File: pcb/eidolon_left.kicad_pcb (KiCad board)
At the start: 2 copper layers, 117.1 x 83.9 mm, 37 parts

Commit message: fix(pcb): land faithfully re-routed boards + gerbers (corrected pinout)
Replace the old buggy routed boards with the re-routed eidolon_{left,right}
from the phantom autorouter (~/git/phantom-router), built on the corrected
XIAO right-column pinout. Both halves: 0 DRC violations, 0 unconnected.

Whole-module GND pour keepout; explicit hand-shaped B.Cu GND margin rail;
R2/R3 re-derived for the moved pinout (rail crossings on F.Cu, minimal vias);
the mirrored right half's forced GND/RAW crossing and under-MCU access-pad
jumper threaded with one via each. Re-exported gerbers (all layers + drill).

Fab-ready.

Co-Authored-By: Claude Opus 4.8 <noreply@anthropic.com>
Claude-Session: https://claude.ai/code/session_01MD1mhgQXFf8iwVCJGWMS4x
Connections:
- MCU1 pad 10: P3V3 -> D9
- MCU1 pad 12: D9 -> P3V3
- MCU1 pad 13: R3 -> GND
- MCU1 pad 14: R2 -> P5V
- MCU1 pad 8: P5V -> R2
- MCU1 pad 9: GND -> R3
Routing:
- net R2: track 129.9 -> 114.6 mm, vias 1 -> 2
- net R3: track 89.1 -> 80.0 mm, vias 1 -> 2
- net GND: track 159.7 -> 164.2 mm

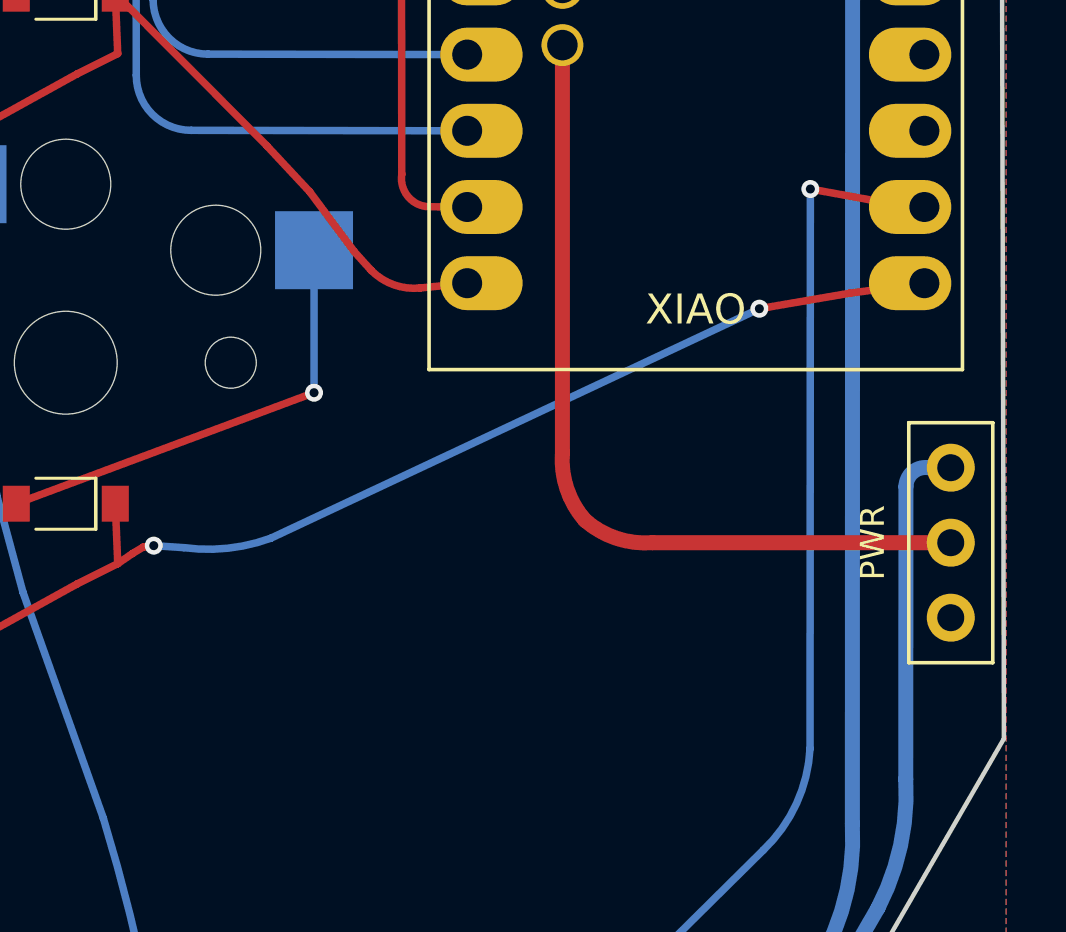
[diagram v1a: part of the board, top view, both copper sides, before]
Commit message: feat(pcb): per-half XIAO pin maps; declutter right-half routing
Each half is an independent wireless unit, so the net->pin maps need not match.
Give the right half its own map (all 4 rows on the matrix-facing D7-D10 edge:
D7:R3 D8:R2 D9:R1 D10:R0; columns on D0-D4). The left keeps R0/R1 on D5/D6.

This moves R0/R1 off the far MCU edge on the right, so they fan out directly
east instead of crossing back over the MCU ("west-about" boxed routes). Only
the 5 columns now cross under the MCU on the right (the physical floor). Both
halves re-routed to 0 DRC / 0 unconnected; gerbers re-exported.

FIRMWARE: the halves now use different MATRIX_ROW_PINS (left D5-D8, right
D7-D10) -- update each half's kscan/matrix map accordingly.

Co-Authored-By: Claude Opus 4.8 <noreply@anthropic.com>
Claude-Session: https://claude.ai/code/session_01MD1mhgQXFf8iwVCJGWMS4x
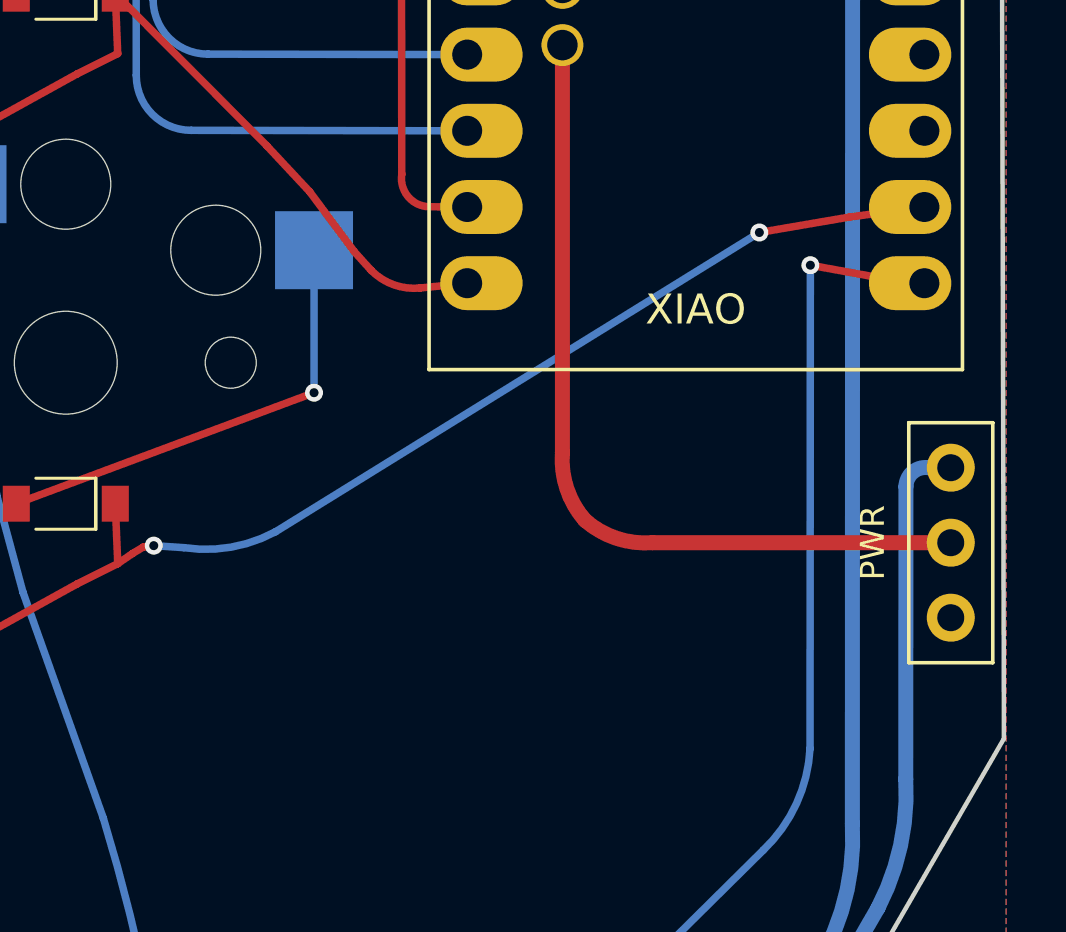
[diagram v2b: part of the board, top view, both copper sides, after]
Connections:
- MCU1 pad 8: R2 -> R3
- MCU1 pad 9: R3 -> R2
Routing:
- net R3: track 80.0 -> 77.5 mm
- net R2: track 114.6 -> 115.7 mm
